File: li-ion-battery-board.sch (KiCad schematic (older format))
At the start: 11 parts

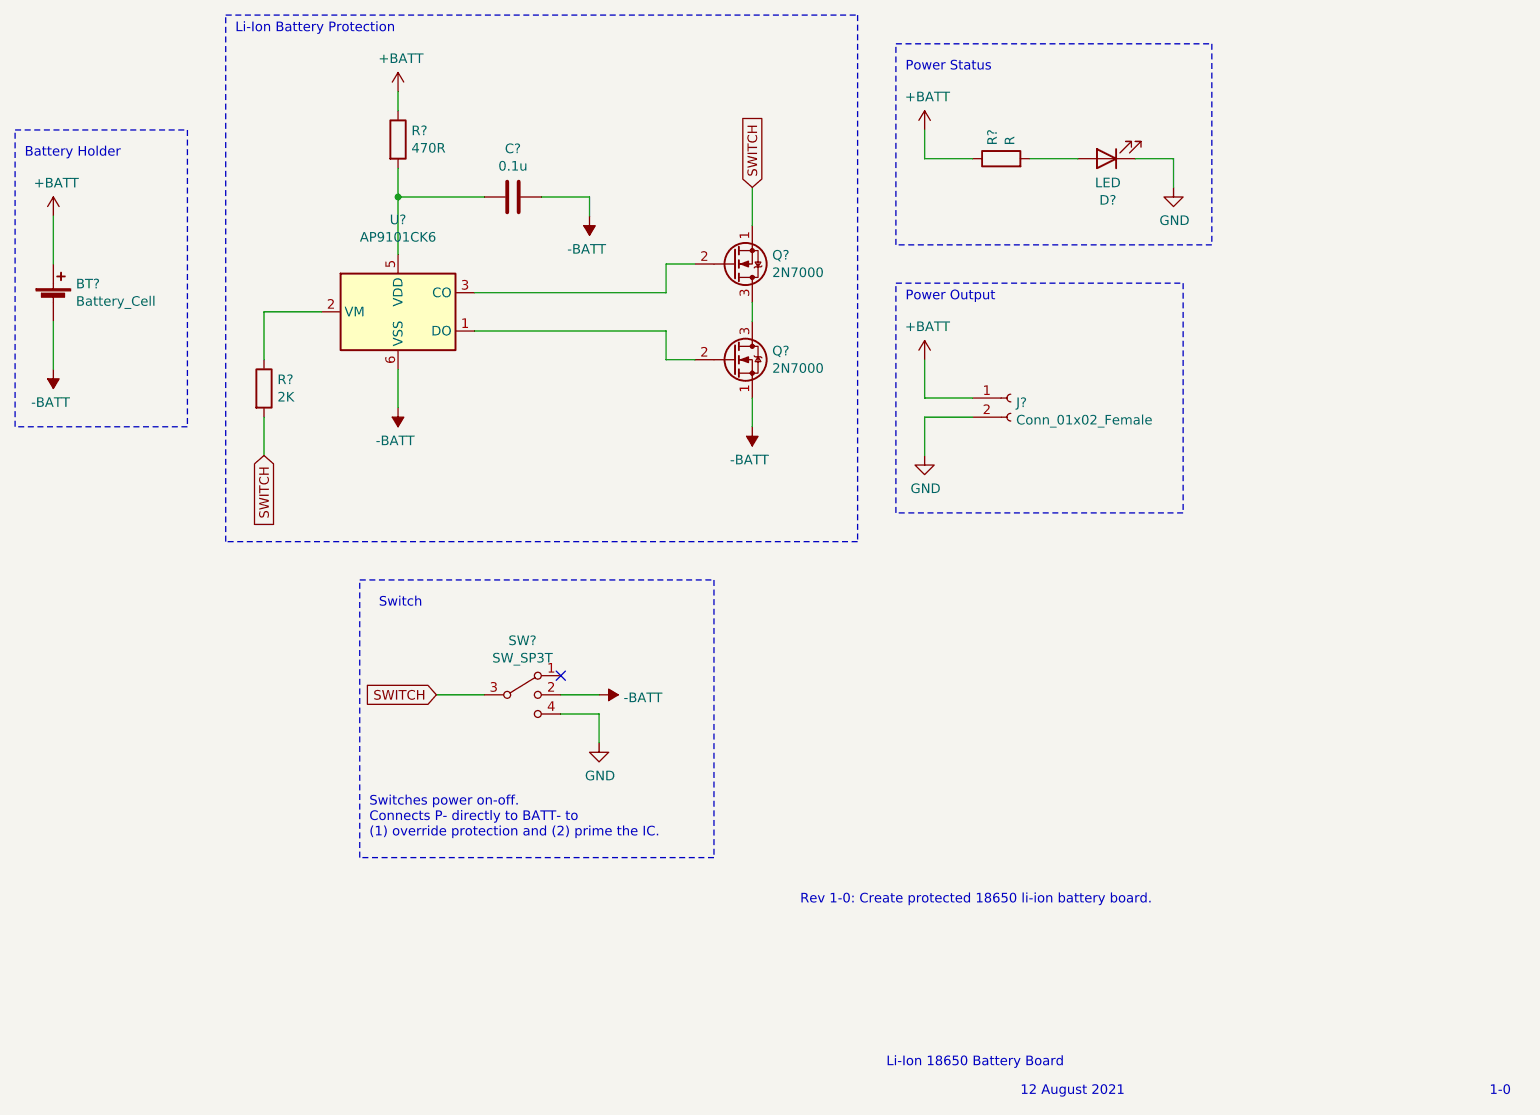
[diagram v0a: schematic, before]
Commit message: Assign footprints in schematic.
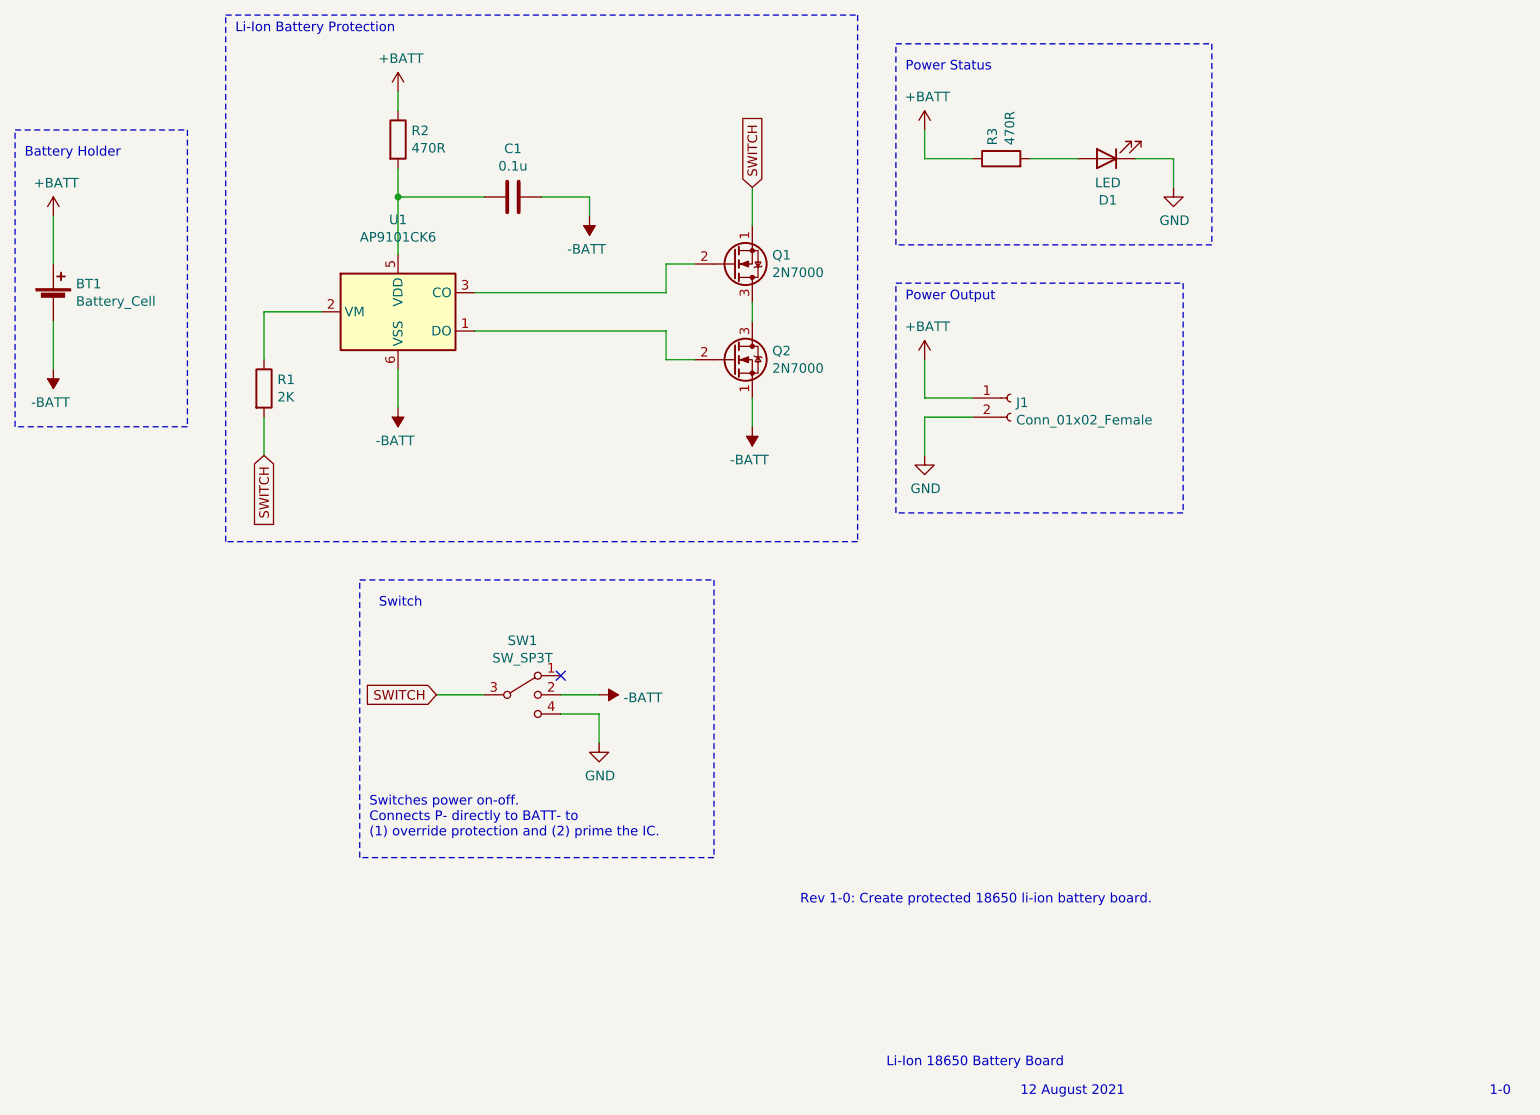
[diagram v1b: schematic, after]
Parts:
- BT1: renamed from BT?; footprint (none) -> electronics-li-ion-battery-board:BatteryHolder_CZK_1x18650
- C1: renamed from C?; footprint (none) -> Capacitor_SMD:C_1206_3216Metric_Pad1.33x1.80mm_HandSolder
- D1: renamed from D?; footprint (none) -> LED_SMD:LED_1206_3216Metric_Castellated
- J1: renamed from J?; footprint (none) -> electronics-li-ion-battery-board:Castellation_1x02_P2.54mm_Vertical
- R1, R2: renamed from R?; footprint (none) -> Resistor_SMD:R_1206_3216Metric_Pad1.30x1.75mm_HandSolder
- R3: renamed from R?; value R -> 470R; footprint (none) -> Resistor_SMD:R_1206_3216Metric_Pad1.30x1.75mm_HandSolder
- SW1: renamed from SW?; footprint (none) -> electronics-li-ion-battery-board:SW_SP3T_Nidec_CL_SB_13B
- gave numbers to parts that had none: 3
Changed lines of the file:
@@
 Rev 1-0: Create protected 18650 li-ion battery board.
 $Comp
-L Connector:Conn_01x02_Female J?
+L Connector:Conn_01x02_Female J1
 U 1 1 6115E3AB
 P 8100 4000
-F 0 "J?" H 8128 3976 50  0000 L CNN
+F 0 "J1" H 8128 3976 50  0000 L CNN
 F 1 "Conn_01x02_Female" H 8128 3885 50  0000 L CNN
-F 2 "" H 8100 4000 50  0001 C CNN
+F 2 "electronics-li-ion-battery-board:Castellation_1x02_P2.54mm_Vertical" H 8100 4000 50  0001 C CNN
 F 3 "~" H 8100 4000 50  0001 C CNN
 	1    8100 4000
@@
 $EndComp
 $Comp
-L Battery_Management:AP9101CK6 U?
+L Battery_Management:AP9101CK6 U1
 U 1 1 6115F741
 P 4900 3550
-F 0 "U?" H 4900 4031 50  0000 C CNN
+F 0 "U1" H 4900 4031 50  0000 C CNN
 F 1 "AP9101CK6" H 4900 3940 50  0000 C CNN
 F 2 "Package_TO_SOT_SMD:SOT-23-6" H 4900 3550 50  0001 C CNN
@@
 $EndComp
 $Comp
-L Device:R R?
+L Device:R R1
 U 1 1 6116037C
 P 4200 3950
-F 0 "R?" H 4270 3996 50  0000 L CNN
+F 0 "R1" H 4270 3996 50  0000 L CNN
 F 1 "2K" H 4270 3905 50  0000 L CNN
-F 2 "" V 4130 3950 50  0001 C CNN
+F 2 "Resistor_SMD:R_1206_3216Metric_Pad1.30x1.75mm_HandSolder" V 4130 3950 50  0001 C CNN
 F 3 "~" H 4200 3950 50  0001 C CNN
 	1    4200 3950
@@
 $EndComp
 $Comp
-L Device:R R?
+L Device:R R2
 U 1 1 611604C2
 P 4900 2650
-F 0 "R?" H 4970 2696 50  0000 L CNN
+F 0 "R2" H 4970 2696 50  0000 L CNN
 F 1 "470R" H 4970 2605 50  0000 L CNN
-F 2 "" V 4830 2650 50  0001 C CNN
+F 2 "Resistor_SMD:R_1206_3216Metric_Pad1.30x1.75mm_HandSolder" V 4830 2650 50  0001 C CNN
 F 3 "~" H 4900 2650 50  0001 C CNN
 	1    4900 2650
@@
 $EndComp
 $Comp
-L Device:C C?
+L Device:C C1
 U 1 1 6116093E
 P 5500 2950
-F 0 "C?" V 5248 2950 50  0000 C CNN
+F 0 "C1" V 5248 2950 50  0000 C CNN
 F 1 "0.1u" V 5339 2950 50  0000 C CNN
-F 2 "" H 5538 2800 50  0001 C CNN
+F 2 "Capacitor_SMD:C_1206_3216Metric_Pad1.33x1.80mm_HandSolder" H 5538 2800 50  0001 C CNN
 F 3 "~" H 5500 2950 50  0001 C CNN
 	1    5500 2950
@@
 $EndComp
 $Comp
-L Transistor_FET:2N7000 Q?
+L Transistor_FET:2N7000 Q2
 U 1 1 61161C15
 P 6650 3800
-F 0 "Q?" H 6854 3846 50  0000 L CNN
+F 0 "Q2" H 6854 3846 50  0000 L CNN
 F 1 "2N7000" H 6854 3755 50  0000 L CNN
 F 2 "Package_TO_SOT_THT:TO-92_Inline" H 6850 3725 50  0001 L CIN
@@
 $EndComp
 $Comp
-L Device:LED D?
+L Device:LED D1
 U 1 1 611625DD
 P 8600 2750
-F 0 "D?" H 8593 2967 50  0000 C CNN
+F 0 "D1" H 8593 2967 50  0000 C CNN
 F 1 "LED" H 8593 2876 50  0000 C CNN
-F 2 "" H 8600 2750 50  0001 C CNN
+F 2 "LED_SMD:LED_1206_3216Metric_Castellated" H 8600 2750 50  0001 C CNN
 F 3 "~" H 8600 2750 50  0001 C CNN
 	1    8600 2750
@@
 $EndComp
 $Comp
-L Device:R R?
+L Device:R R3
 U 1 1 611633C6
 P 8050 2750
-F 0 "R?" H 8120 2796 50  0000 L CNN
-F 1 "R" H 8120 2705 50  0000 L CNN
-F 2 "" V 7980 2750 50  0001 C CNN
+F 0 "R3" H 8120 2796 50  0000 L CNN
+F 1 "470R" H 8120 2705 50  0000 L CNN
+F 2 "Resistor_SMD:R_1206_3216Metric_Pad1.30x1.75mm_HandSolder" V 7980 2750 50  0001 C CNN
 F 3 "~" H 8050 2750 50  0001 C CNN
 	1    8050 2750
@@
 $EndComp
 $Comp
-L Device:Battery_Cell BT?
+L Device:Battery_Cell BT1
 U 1 1 61163E17
 P 3100 3500
-F 0 "BT?" H 3218 3596 50  0000 L CNN
+F 0 "BT1" H 3218 3596 50  0000 L CNN
 F 1 "Battery_Cell" H 3218 3505 50  0000 L CNN
-F 2 "" V 3100 3560 50  0001 C CNN
+F 2 "electronics-li-ion-battery-board:BatteryHolder_CZK_1x18650" V 3100 3560 50  0001 C CNN
 F 3 "~" V 3100 3560 50  0001 C CNN
 	1    3100 3500
@@
 $EndComp
 $Comp
-L Switch:SW_SP3T SW?
+L Switch:SW_SP3T SW1
 U 1 1 6116450A
 P 5550 5550
-F 0 "SW?" H 5550 5833 50  0000 C CNN
+F 0 "SW1" H 5550 5833 50  0000 C CNN
 F 1 "SW_SP3T" H 5550 5742 50  0000 C CNN
-F 2 "" H 4925 5725 50  0001 C CNN
+F 2 "electronics-li-ion-battery-board:SW_SP3T_Nidec_CL_SB_13B" H 4925 5725 50  0001 C CNN
 F 3 "~" H 4925 5725 50  0001 C CNN
 	1    5550 5550
@@
 $EndComp
 $Comp
-L power:-BATT #PWR?
+L power:-BATT #PWR02
 U 1 1 6116A641
 P 3100 3850
-F 0 "#PWR?" H 3100 3700 50  0001 C CNN
+F 0 "#PWR02" H 3100 3700 50  0001 C CNN
 F 1 "-BATT" H 3115 4023 50  0000 C CNN
 F 2 "" H 3100 3850 50  0001 C CNN
@@
 	8200 2750 8450 2750
 $Comp
-L power:-BATT #PWR?
+L power:-BATT #PWR04
 U 1 1 6116DF50
 P 4900 4050
-F 0 "#PWR?" H 4900 3900 50  0001 C CNN
+F 0 "#PWR04" H 4900 3900 50  0001 C CNN
 F 1 "-BATT" H 4915 4223 50  0000 C CNN
 F 2 "" H 4900 4050 50  0001 C CNN
@@
 	4900 3850 4900 4050
 $Comp
-L power:GND #PWR?
+L power:GND #PWR011
 U 1 1 6116EA46
 P 7650 4300
-F 0 "#PWR?" H 7650 4050 50  0001 C CNN
+F 0 "#PWR011" H 7650 4050 50  0001 C CNN
 F 1 "GND" H 7655 4127 50  0000 C CNN
 F 2 "" H 7650 4300 50  0001 C CNN
@@
 	7650 4100 7900 4100
 $Comp
-L power:GND #PWR?
+L power:GND #PWR012
 U 1 1 6117146D
 P 8950 2900
-F 0 "#PWR?" H 8950 2650 50  0001 C CNN
+F 0 "#PWR012" H 8950 2650 50  0001 C CNN
 F 1 "GND" H 8955 2727 50  0000 C CNN
 F 2 "" H 8950 2900 50  0001 C CNN
@@
 	4200 4100 4200 4300
 $Comp
-L power:-BATT #PWR?
+L power:-BATT #PWR05
 U 1 1 61175BB5
 P 5900 3050
-F 0 "#PWR?" H 5900 2900 50  0001 C CNN
+F 0 "#PWR05" H 5900 2900 50  0001 C CNN
 F 1 "-BATT" H 5915 3223 50  0000 C CNN
 F 2 "" H 5900 3050 50  0001 C CNN
@@
 	5900 2950 5900 3050
 $Comp
-L Transistor_FET:2N7000 Q?
+L Transistor_FET:2N7000 Q1
 U 1 1 61161D18
 P 6650 3300
-F 0 "Q?" H 6854 3254 50  0000 L CNN
+F 0 "Q1" H 6854 3254 50  0000 L CNN
 F 1 "2N7000" H 6854 3345 50  0000 L CNN
 F 2 "Package_TO_SOT_THT:TO-92_Inline" H 6850 3225 50  0001 L CIN
@@
 $EndComp
 $Comp
-L power:-BATT #PWR?
+L power:-BATT #PWR08
 U 1 1 611803AA
 P 6750 4150
-F 0 "#PWR?" H 6750 4000 50  0001 C CNN
+F 0 "#PWR08" H 6750 4000 50  0001 C CNN
 F 1 "-BATT" H 6765 4323 50  0000 C CNN
 F 2 "" H 6750 4150 50  0001 C CNN
@@
 SWITCH
 $Comp
-L power:GND #PWR?
+L power:GND #PWR07
 U 1 1 6119C681
 P 5950 5800
-F 0 "#PWR?" H 5950 5550 50  0001 C CNN
+F 0 "#PWR07" H 5950 5550 50  0001 C CNN
 F 1 "GND" H 5955 5627 50  0000 C CNN
 F 2 "" H 5950 5800 50  0001 C CNN
@@
 NoConn ~ 5750 5450
 $Comp
-L power:-BATT #PWR?
+L power:-BATT #PWR06
 U 1 1 6119DB9A
 P 5950 5550
-F 0 "#PWR?" H 5950 5400 50  0001 C CNN
+F 0 "#PWR06" H 5950 5400 50  0001 C CNN
 F 1 "-BATT" V 5965 5678 50  0000 L CNN
 F 2 "" H 5950 5550 50  0001 C CNN
@@
 $EndComp
 $Comp
-L power:+BATT #PWR?
+L power:+BATT #PWR01
 U 1 1 6119FD35
 P 3100 3050
-F 0 "#PWR?" H 3100 2900 50  0001 C CNN
+F 0 "#PWR01" H 3100 2900 50  0001 C CNN
 F 1 "+BATT" H 3115 3223 50  0000 C CNN
 F 2 "" H 3100 3050 50  0001 C CNN
@@
 $EndComp
 $Comp
-L power:+BATT #PWR?
+L power:+BATT #PWR09
 U 1 1 611A0718
 P 7650 2600
-F 0 "#PWR?" H 7650 2450 50  0001 C CNN
+F 0 "#PWR09" H 7650 2450 50  0001 C CNN
 F 1 "+BATT" H 7665 2773 50  0000 C CNN
 F 2 "" H 7650 2600 50  0001 C CNN
@@
 $EndComp
 $Comp
-L power:+BATT #PWR?
+L power:+BATT #PWR03
 U 1 1 611A14BD
 P 4900 2400
-F 0 "#PWR?" H 4900 2250 50  0001 C CNN
+F 0 "#PWR03" H 4900 2250 50  0001 C CNN
 F 1 "+BATT" H 4915 2573 50  0000 C CNN
 F 2 "" H 4900 2400 50  0001 C CNN
@@
 $EndComp
 $Comp
-L power:+BATT #PWR?
+L power:+BATT #PWR010
 U 1 1 611A2013
 P 7650 3800
-F 0 "#PWR?" H 7650 3650 50  0001 C CNN
+F 0 "#PWR010" H 7650 3650 50  0001 C CNN
 F 1 "+BATT" H 7665 3973 50  0000 C CNN
 F 2 "" H 7650 3800 50  0001 C CNN

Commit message: Change MOSFET pin and layout assignments.
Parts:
- Q1, Q2: value 2N7000 -> MOSFET; footprint Package_TO_SOT_THT:TO-92_Inline -> Package_TO_SOT_SMD:SOT-23; symbol Transistor_FET:2N7000 -> Transistor_FET:2N7002
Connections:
- net -BATT: now also Q2.2 (S); no longer Q2.1 (S)
- net SWITCH: now also Q1.2 (S); no longer Q1.1 (S)
- net at U1.1 (DO): now also Q2.1 (G); no longer Q2.2 (G)
- net at U1.3 (CO): now also Q1.1 (G); no longer Q1.2 (G)
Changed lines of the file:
@@
 $EndComp
 $Comp
-L Transistor_FET:2N7000 Q2
+L Transistor_FET:2N7002 Q2
 U 1 1 61161C15
 P 6650 3800
 F 0 "Q2" H 6854 3846 50  0000 L CNN
-F 1 "2N7000" H 6854 3755 50  0000 L CNN
-F 2 "Package_TO_SOT_THT:TO-92_Inline" H 6850 3725 50  0001 L CIN
+F 1 "MOSFET" H 6854 3755 50  0000 L CNN
+F 2 "Package_TO_SOT_SMD:SOT-23" H 6850 3725 50  0001 L CIN
 F 3 "https://www.onsemi.com/pub/Collateral/NDS7002A-D.PDF" H 6650 3800 50  0001 L CNN
 	1    6650 3800
@@
 	5900 2950 5900 3050
 $Comp
-L Transistor_FET:2N7000 Q1
+L Transistor_FET:2N7002 Q1
 U 1 1 61161D18
 P 6650 3300
 F 0 "Q1" H 6854 3254 50  0000 L CNN
-F 1 "2N7000" H 6854 3345 50  0000 L CNN
-F 2 "Package_TO_SOT_THT:TO-92_Inline" H 6850 3225 50  0001 L CIN
+F 1 "MOSFET" H 6854 3345 50  0000 L CNN
+F 2 "Package_TO_SOT_SMD:SOT-23" H 6850 3225 50  0001 L CIN
 F 3 "https://www.onsemi.com/pub/Collateral/NDS7002A-D.PDF" H 6650 3300 50  0001 L CNN
 	1    6650 3300

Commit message: Complete PCB layout.
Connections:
- net SWITCH: now also SW1.1
- no-connect marks 1 -> 0
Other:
- note added: "Switches power on-off.\nConnects P- directly to BATT- \nto prime the IC."
- note removed: "Switches power on-off.\nConnects P- directly to BATT- to \n(1) override protection and (2) prime the IC."
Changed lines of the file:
@@
 Wire Wire Line
 	5950 5650 5950 5800
-NoConn ~ 5750 5450
 $Comp
 L power:-BATT #PWR06
@@
 Text Notes 4800 5100 0    50   ~ 0
 Switch
-Text Notes 4750 6300 0    50   ~ 0
-Switches power on-off.\nConnects P- directly to BATT- to \n(1) override protection and (2) prime the IC.
 Text Notes 2950 2750 0    50   ~ 0
 Battery Holder
@@
 Wire Notes Line
 	4700 6400 4700 4950
+Text Notes 4750 6300 0    50   ~ 0
+Switches power on-off.\nConnects P- directly to BATT- \nto prime the IC.
+Text GLabel 5950 5450 2    50   Input ~ 0
+SWITCH
+Wire Wire Line
+	5750 5450 5950 5450
 $EndSCHEMATC
